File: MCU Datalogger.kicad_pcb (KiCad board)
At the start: 2 copper layers, 45 x 40 mm, 29 parts, among them J1 Conn_01x04_Pin, J2 Conn_01x04_Pin, J3 Conn_01x09_Pin, J4 Conn_02x03_Odd_Even, U1 24LC1025, U2 24LC1025, U3 DS1337S_, U4 ATMEGA328P-AU, Y1 32.768 KHz, Y2 16 MHz

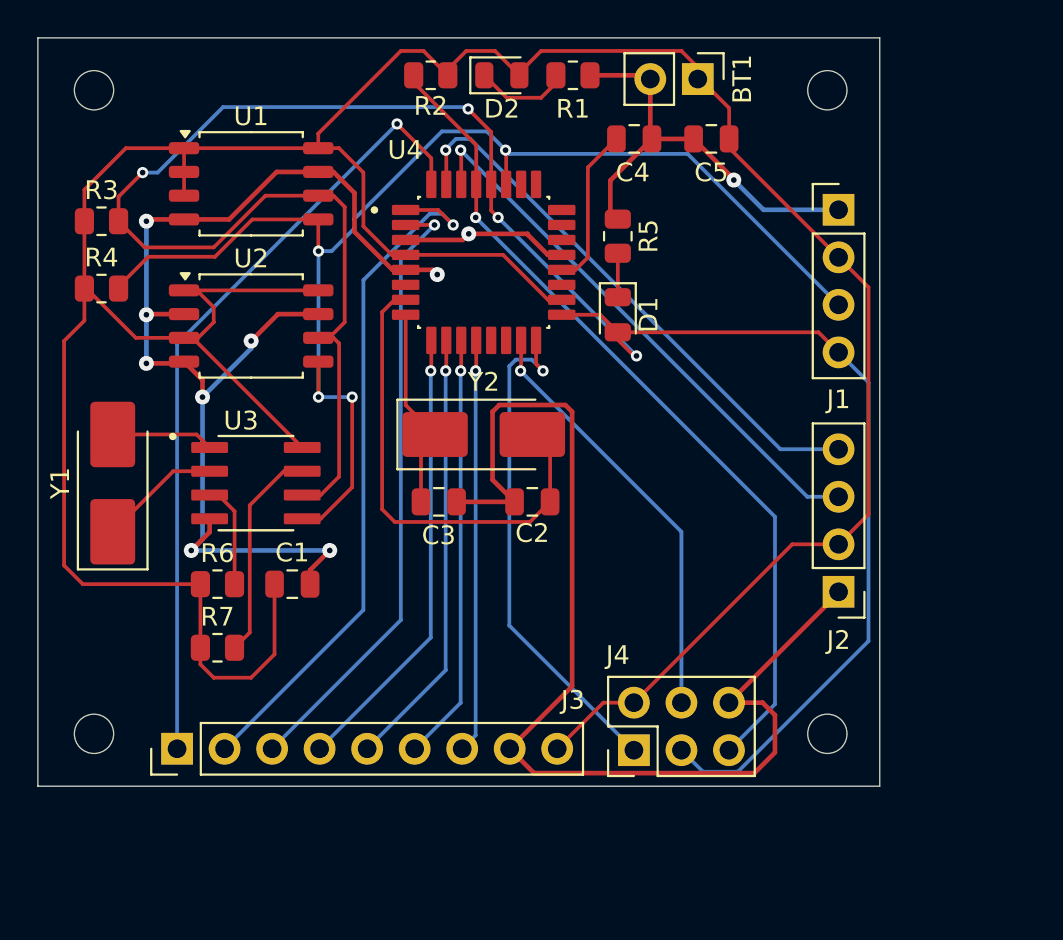
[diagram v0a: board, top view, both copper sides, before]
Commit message: Re-design 2 layer board
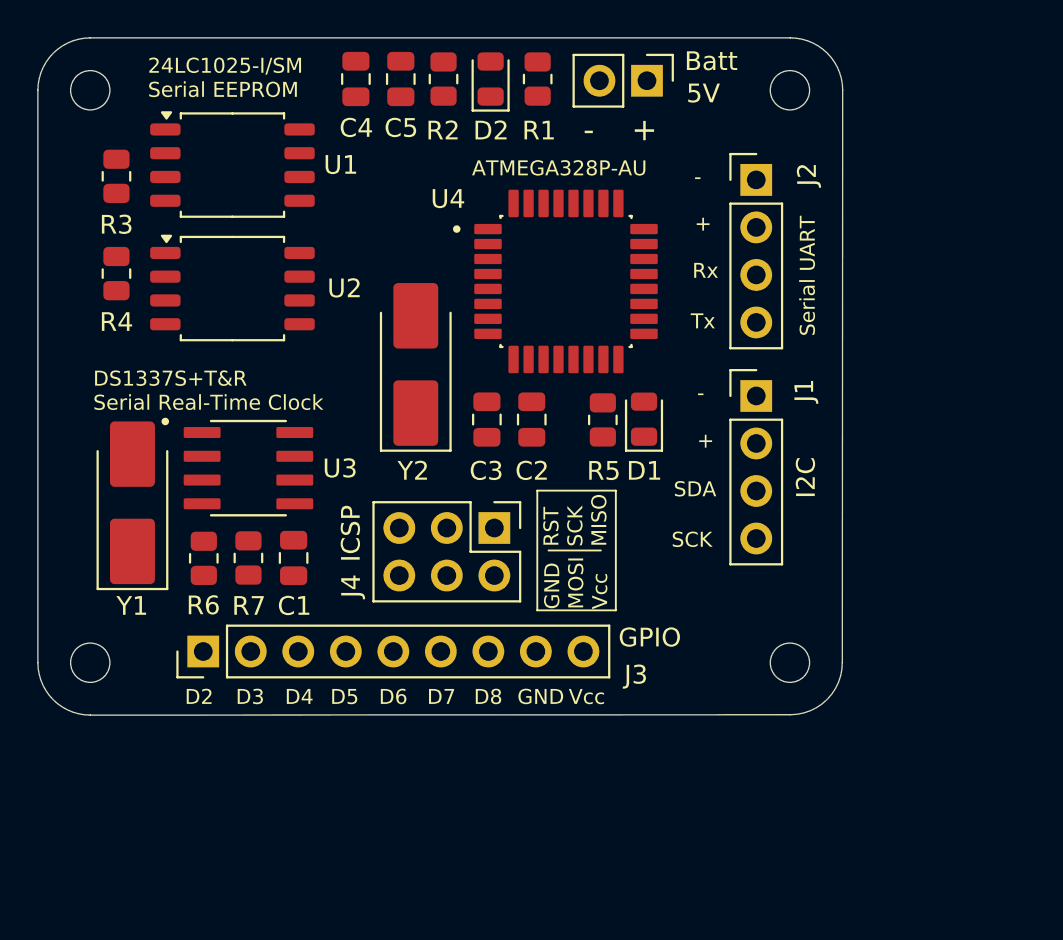
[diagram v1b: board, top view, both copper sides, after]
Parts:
- moved J2 22.5 mm to (153.0, 81.4), turned to 0 degrees
- moved C5 16.9 mm to (134.0, 76.0), turned to -90 degrees
- moved C4 15.2 mm to (131.6, 76.0), turned to 90 degrees
- moved J4 14.0 mm to (139.0, 100.0), turned to -90 degrees
- moved J1 10.9 mm to (153.0, 92.9)
- moved R5 9.85 mm to (144.8, 94.2)
- moved D1 5.75 mm to (147.0, 94.2), turned to 90 degrees
- moved J3 5.39 mm to (123.4, 106.6)
- moved Y2 5.22 mm to (134.8, 91.3), turned to 90 degrees
- moved C3 5.10 mm to (138.6, 94.2), turned to -90 degrees
- moved R7 5.08 mm to (125.9, 101.6), turned to 90 degrees
- moved U4 4.52 mm to (142.8, 86.8)
- moved C2 4.40 mm to (141.0, 94.2), turned to -90 degrees
- moved H4 4.29 mm to (154.8, 107.2)
- moved H3 3.81 mm to (117.4, 107.2)
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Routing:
- net /Vcc: track 177.4 -> 0.00 mm
- net GND: track 155.5 -> 0.00 mm, vias 10 -> 0
- net /SCK: track 119.1 -> 0.00 mm, vias 4 -> 0
- net /SDA: track 70.1 -> 0.00 mm, vias 4 -> 0
- net /RESET: track 45.1 -> 0.00 mm, vias 1 -> 0
- net /D2: track 42.3 -> 0.00 mm, vias 1 -> 0
- net /D3: track 37.5 -> 0.00 mm, vias 1 -> 0
- net /D4: track 33.1 -> 0.00 mm, vias 1 -> 0
- net /TX: track 30.0 -> 0.00 mm, vias 1 -> 0
- net /RX: track 29.7 -> 0.00 mm, vias 1 -> 0
- net /MISO: track 27.3 -> 0.00 mm, vias 1 -> 0
- net Net-(U4-PB6): track 25.8 -> 0.00 mm
- net /D5: track 24.3 -> 0.00 mm, vias 1 -> 0
- net /D6: track 23.6 -> 0.00 mm, vias 1 -> 0
- net /MOSI: track 22.9 -> 0.00 mm, vias 1 -> 0
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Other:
- board size 45 x 40 mm -> 43 x 36.2 mm
- board text added: "+"
- board text added: "-"
- board text added: "24LC1025-I/SM Serial EEPROM"
- board text added: "5V"
- board text added: "ATMEGA328P-AU"
- board text added: "Batt"
- board text added: "D2"
- board text added: "D3"
- board text added: "D4"
- board text added: "D5"
- board text added: "D6"
- board text added: "D7"
- board text added: "D8"
- board text added: "DS1337S+T&R Serial Real-Time Clock"
- board text added: "GND"
- board text added: "GPIO"
- board text added: "I2C"
- board text added: "ICSP"
- board text added: "MISO"
- board text added: "MOSI"
- board text added: "RST"
- board text added: "Rx"
- board text added: "SCK"
- board text added: "SDA"
- board text added: "Serial UART"
- board text added: "Tx"
- board text added: "Vcc"

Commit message: save changes
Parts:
- moved BT1 0.32 mm to (147.2, 76.4)
- moved C4 0.32 mm to (131.7, 76.3)
- moved C5 0.32 mm to (134.1, 76.3)
- moved D2 0.32 mm to (138.9, 76.3)
- moved R1 0.32 mm to (141.4, 76.3)
- moved R2 0.32 mm to (136.3, 76.3)
- moved R3 0.30 mm to (118.5, 81.2)
- moved R4 0.30 mm to (118.5, 86.4)
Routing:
- net GND: track 0.00 -> 103.4 mm, vias 0 -> 5
- net /SCK: track 0.00 -> 101.7 mm, vias 0 -> 6
- net /SDA: track 0.00 -> 78.3 mm, vias 0 -> 5
- net /Vcc: track 0.00 -> 71.5 mm, vias 0 -> 2
- net /D2: track 0.00 -> 34.0 mm, vias 0 -> 1
- net /RESET: track 0.00 -> 32.9 mm, vias 0 -> 1
- net /D3: track 0.00 -> 31.4 mm, vias 0 -> 1
- net /D5: track 0.00 -> 29.8 mm, vias 0 -> 1
- net /D4: track 0.00 -> 28.3 mm, vias 0 -> 1
- net /D6: track 0.00 -> 27.6 mm, vias 0 -> 1
- net Net-(U4-PB6): track 0.00 -> 27.0 mm
- net /MOSI: track 0.00 -> 26.3 mm, vias 0 -> 2
- net /D7: track 0.00 -> 25.4 mm, vias 0 -> 1
- net /D8: track 0.00 -> 23.1 mm, vias 0 -> 1
- net Net-(U4-AREF): track 0.00 -> 21.5 mm, vias 0 -> 2
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- added copper zone on F.Cu, net /Vcc
- added copper zone on B.Cu, net GND

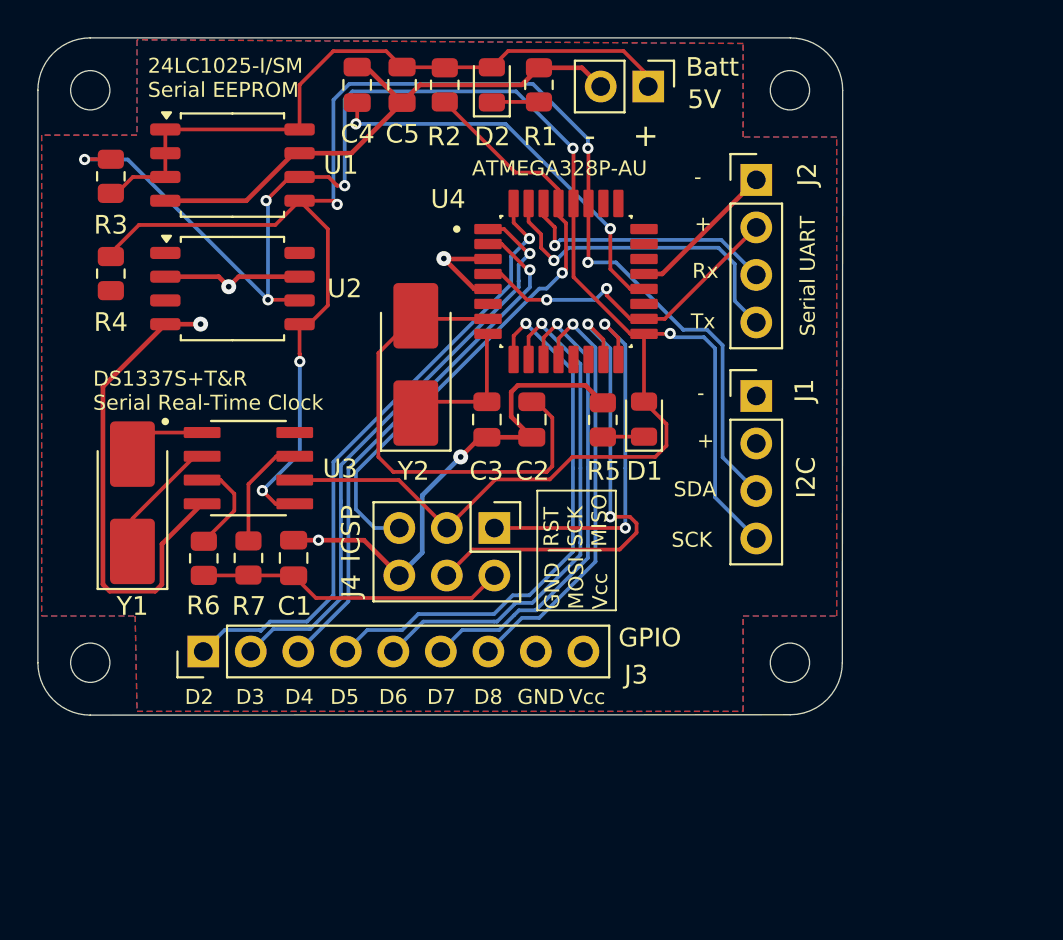
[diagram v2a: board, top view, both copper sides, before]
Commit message: fix DRC error
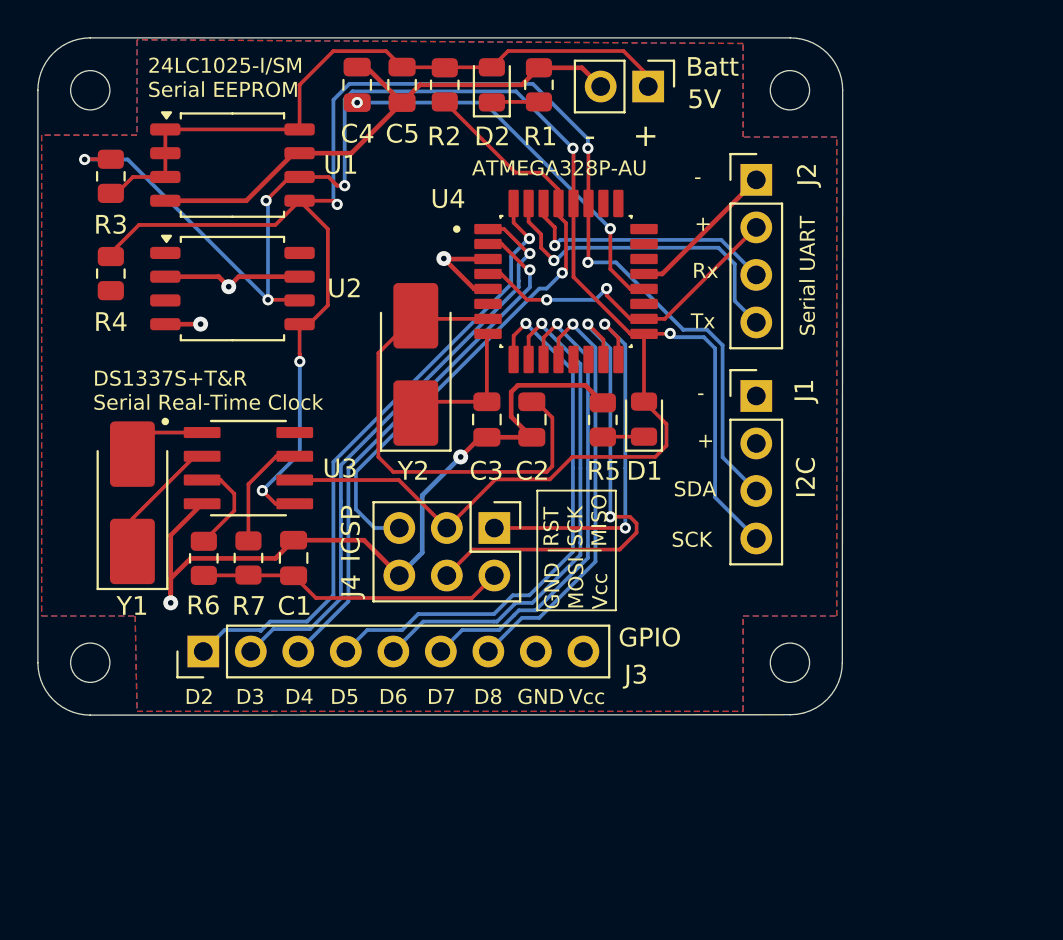
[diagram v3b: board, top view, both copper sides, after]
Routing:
- net GND: track 103.4 -> 94.2 mm
- net Net-(U4-AREF): track 21.5 -> 20.7 mm

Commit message: Updates
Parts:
- moved J3 14.0 mm to (133.2, 116.6)
- moved U1 14.0 mm to (134.8, 90.6)
- moved BT1 14.0 mm to (157.0, 86.4)
- moved C2 14.0 mm to (150.8, 104.2)
- moved C3 14.0 mm to (148.4, 104.2)
- moved C4 14.0 mm to (141.4, 86.3)
- moved C5 14.0 mm to (143.8, 86.3)
- moved D1 14.0 mm to (156.8, 104.2)
- moved H1 14.0 mm to (127.2, 86.6)
- moved J1 14.0 mm to (162.8, 103.0)
- moved J2 14.0 mm to (162.8, 91.4)
- moved J4 14.0 mm to (148.8, 110.0)
- moved R1 14.0 mm to (151.2, 86.3)
- moved R2 14.0 mm to (146.1, 86.3)
- moved R3 14.0 mm to (128.3, 91.2)
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
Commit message: fixed routing bug
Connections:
- net /SCK renamed /SCL
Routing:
- net /SCL: track 101.7 -> 97.8 mm, vias 6 -> 5
